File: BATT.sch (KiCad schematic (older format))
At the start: 7 parts

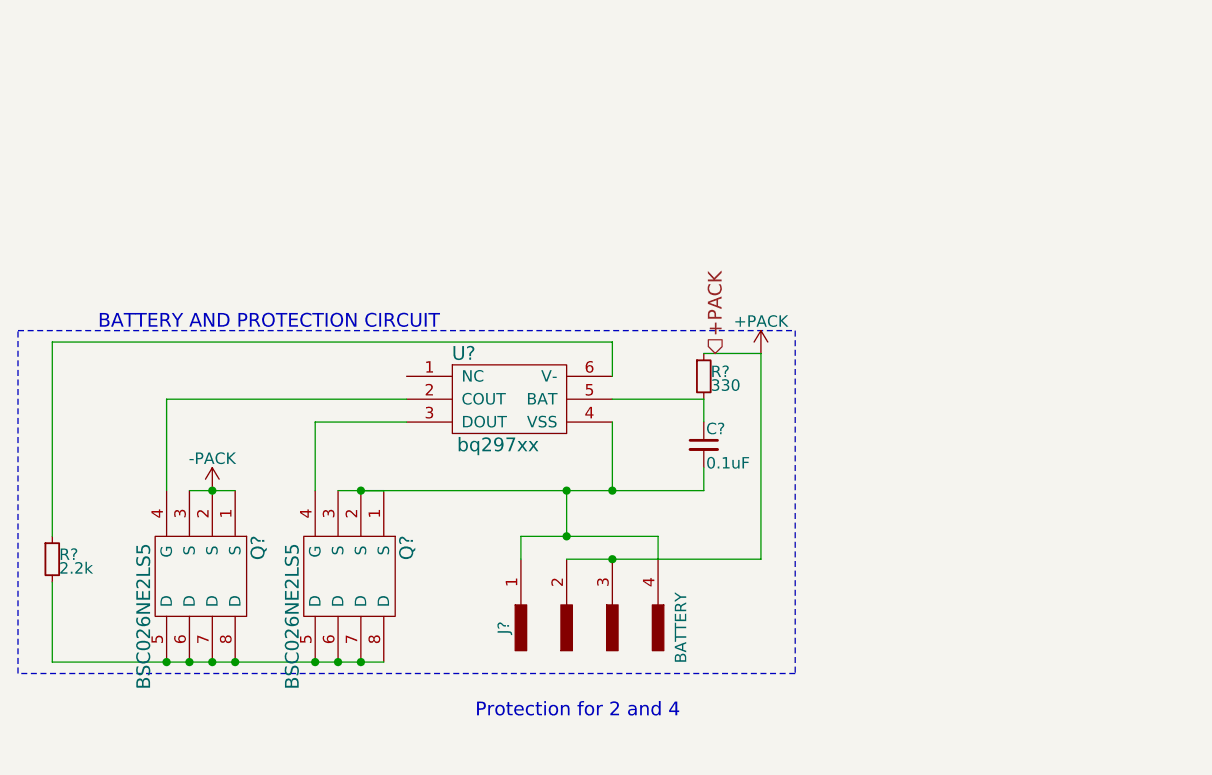
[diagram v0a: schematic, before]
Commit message: (Confirmation) BPack Ammeter + Proctection Circuit Edit
Making sure the last commit pushed all edits.
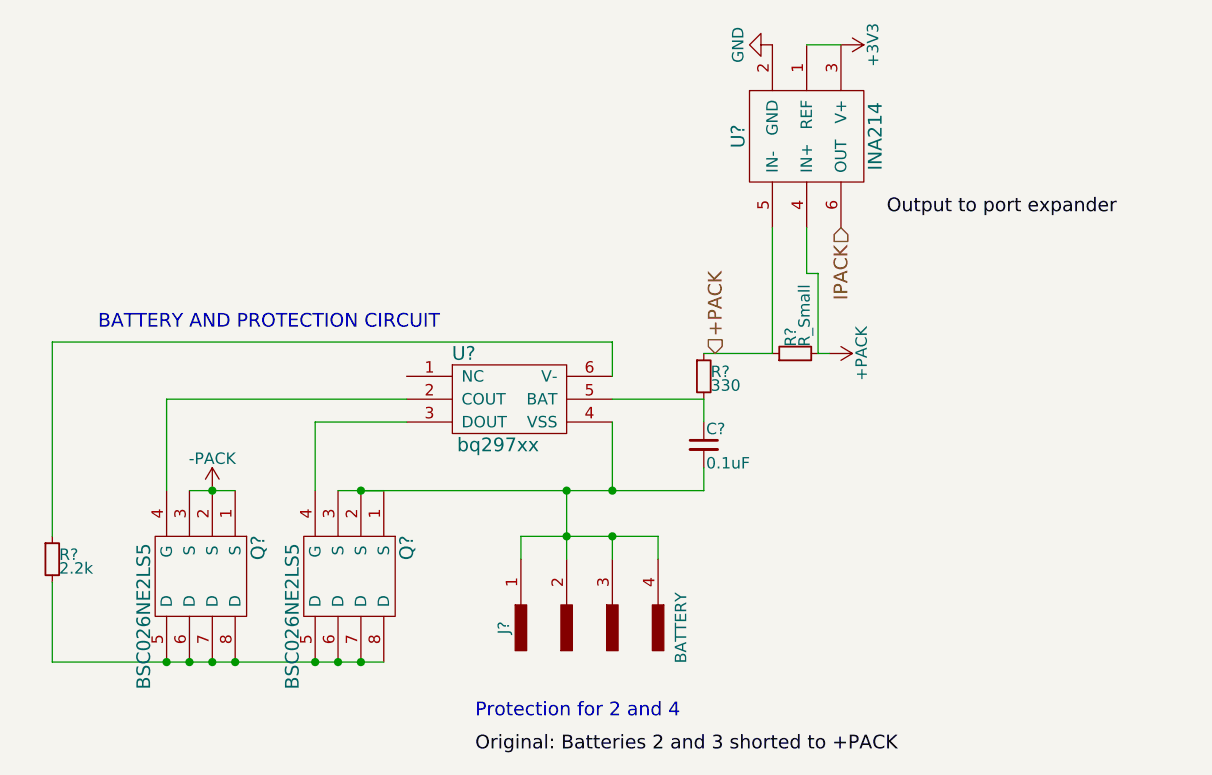
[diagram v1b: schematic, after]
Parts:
- added R?: R_Small, symbol R_Small
- added U?: INA214, symbol INA214
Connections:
- net +PACK: now also R?.1, R?.2, U?.4 (IN+), U?.5 (IN-); no longer J?.2, J?.3
- net at C?.2, J?.1, J?.4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: now also J?.2, J?.3
- new net +3V3: U?.1 (REF), U?.3 (V+)
- new net GND: U?.2 (GND)
- new net IPACK: U?.6 (OUT)
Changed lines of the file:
@@
 L +PACK #PWR?
 U 1 1 59EA52CA
-P 6750 2550
-F 0 "#PWR?" H 6750 2400 50  0001 C CNN
-F 1 "+PACK" H 6750 2690 50  0000 C CNN
-F 2 "" H 6750 2550 50  0001 C CNN
-F 3 "" H 6750 2550 50  0001 C CNN
-	1    6750 2550
-	1    0    0    -1
+P 7050 2550
+F 0 "#PWR?" H 7050 2400 50  0001 C CNN
+F 1 "+PACK" H 7050 2690 50  0000 C CNN
+F 2 "" H 7050 2550 50  0001 C CNN
+F 3 "" H 7050 2550 50  0001 C CNN
+	1    7050 2550
+	0    1    1    0
 $EndComp
 Text Notes 3850 2450 0    60   ~ 0
@@
 	6100 2500 6100 2650
 Wire Wire Line
-	5900 3150 5900 3350
+	5900 3150 5900 3450
 Connection ~ 5900 3150
-Wire Wire Line
-	6750 3450 6750 2550
-Wire Wire Line
-	6750 2550 6500 2550
-Connection ~ 6100 3450
 Wire Wire Line
 	6100 2850 6100 3150
 Connection ~ 6100 3150
-Wire Notes Line
-	3500 3950 3500 2450
-Wire Notes Line
-	3500 2450 6900 2450
-Wire Notes Line
-	6900 2450 6900 3950
-Wire Notes Line
-	6900 3950 3500 3950
-Wire Wire Line
-	5900 3450 6750 3450
 Text HLabel 6550 2550 1    60   Input ~ 0
 +PACK
 Text Notes 5500 4150 0    60   ~ 0
 Protection for 2 and 4
+$Comp
+L INA214 U?
+U 1 1 5A10F7B5
+P 6950 1600
+F 0 "U?" H 6950 1300 60  0000 C CNN
+F 1 "INA214" H 6950 1900 60  0000 C CNN
+F 2 "" H 6950 1900 60  0001 C CNN
+F 3 "" H 6950 1900 60  0001 C CNN
+	1    6950 1600
+	0    1    1    0
+$EndComp
+Text Label 5500 4300 0    60   ~ 0
+Original: Batteries 2 and 3 shorted to +PACK
+Wire Wire Line
+	6100 3350 6100 3450
+Connection ~ 6100 3350
+$Comp
+L R_Small R?
+U 1 1 5A112EB5
+P 6900 2550
+F 0 "R?" H 6930 2570 50  0000 L CNN
+F 1 "R_Small" H 6930 2510 50  0000 L CNN
+F 2 "" H 6900 2550 50  0001 C CNN
+F 3 "" H 6900 2550 50  0001 C CNN
+	1    6900 2550
+	0    -1   -1   0
+$EndComp
+Wire Wire Line
+	7000 2550 7050 2550
+Wire Wire Line
+	6500 2550 6800 2550
+Wire Wire Line
+	6800 2550 6800 2000
+Wire Wire Line
+	6950 1200 7100 1200
+$Comp
+L +3V3 #PWR?
+U 1 1 5A113C8A
+P 7100 1200
+F 0 "#PWR?" H 7100 1050 50  0001 C CNN
+F 1 "+3V3" H 7100 1340 50  0000 C CNN
+F 2 "" H 7100 1200 50  0001 C CNN
+F 3 "" H 7100 1200 50  0001 C CNN
+	1    7100 1200
+	0    1    1    0
+$EndComp
+$Comp
+L GND #PWR?
+U 1 1 5A113CE6
+P 6800 1200
+F 0 "#PWR?" H 6800 950 50  0001 C CNN
+F 1 "GND" H 6800 1050 50  0000 C CNN
+F 2 "" H 6800 1200 50  0001 C CNN
+F 3 "" H 6800 1200 50  0001 C CNN
+	1    6800 1200
+	0    1    1    0
+$EndComp
+Wire Wire Line
+	7000 2550 7000 2200
+Wire Wire Line
+	7000 2200 6950 2200
+Wire Wire Line
+	6950 2200 6950 2000
+Text HLabel 7100 2000 3    60   Input ~ 0
+IPACK
+Text Label 7300 1950 0    60   ~ 0
+Output to port expander
 $EndSCHEMATC

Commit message: Battery Pack Edits
- Fixed hierarchy label errors (output to input)
- Added Voltmeter to Battery Pack Schematic
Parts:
- added C?: C_Small, symbol C_Small
- added R? (x2): R_Small, symbol R_Small
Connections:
- net +PACK: now also R?.1; no longer R?.1, R?.1, U?.5 (IN-)
- net GND: now also C?.1, R?.2
- new net: R?.1, R?.1, U?.5 (IN-)
- new net VPack: C?.2, R?.1, R?.2
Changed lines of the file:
@@
 L +PACK #PWR?
 U 1 1 59EA52CA
-P 7050 2550
-F 0 "#PWR?" H 7050 2400 50  0001 C CNN
-F 1 "+PACK" H 7050 2690 50  0000 C CNN
-F 2 "" H 7050 2550 50  0001 C CNN
-F 3 "" H 7050 2550 50  0001 C CNN
-	1    7050 2550
+P 7550 2550
+F 0 "#PWR?" H 7550 2400 50  0001 C CNN
+F 1 "+PACK" H 7550 2690 50  0000 C CNN
+F 2 "" H 7550 2550 50  0001 C CNN
+F 3 "" H 7550 2550 50  0001 C CNN
+	1    7550 2550
 	0    1    1    0
 $EndComp
 Text Notes 3850 2450 0    60   ~ 0
 BATTERY AND PROTECTION CIRCUIT
+Text HLabel 7550 2550 1    60   Output ~ 0
++PACK
+Text Notes 5500 4150 0    60   ~ 0
+Protection for 2 and 4
+$Comp
+L INA214 U?
+U 1 1 5A10F7B5
+P 6950 1600
+F 0 "U?" H 6950 1300 60  0000 C CNN
+F 1 "INA214" H 6950 1900 60  0000 C CNN
+F 2 "" H 6950 1900 60  0001 C CNN
+F 3 "" H 6950 1900 60  0001 C CNN
+	1    6950 1600
+	0    1    1    0
+$EndComp
+Text Label 5500 4300 0    60   ~ 0
+Original: Batteries 2 and 3 shorted to +PACK
+$Comp
+L R_Small R?
+U 1 1 5A112EB5
+P 6900 2550
+F 0 "R?" H 6930 2570 50  0000 L CNN
+F 1 "R_Small" H 6930 2510 50  0000 L CNN
+F 2 "" H 6900 2550 50  0001 C CNN
+F 3 "" H 6900 2550 50  0001 C CNN
+	1    6900 2550
+	0    -1   -1   0
+$EndComp
+$Comp
+L +3V3 #PWR?
+U 1 1 5A113C8A
+P 7100 1200
+F 0 "#PWR?" H 7100 1050 50  0001 C CNN
+F 1 "+3V3" H 7100 1340 50  0000 C CNN
+F 2 "" H 7100 1200 50  0001 C CNN
+F 3 "" H 7100 1200 50  0001 C CNN
+	1    7100 1200
+	0    1    1    0
+$EndComp
+$Comp
+L GND #PWR?
+U 1 1 5A113CE6
+P 6800 1200
+F 0 "#PWR?" H 6800 950 50  0001 C CNN
+F 1 "GND" H 6800 1050 50  0000 C CNN
+F 2 "" H 6800 1200 50  0001 C CNN
+F 3 "" H 6800 1200 50  0001 C CNN
+	1    6800 1200
+	0    1    1    0
+$EndComp
+Text HLabel 7100 2000 3    60   Input ~ 0
+IPACK
+Text Label 7300 1950 0    60   ~ 0
+Output to port expander
+$Comp
+L R_Small R?
+U 1 1 5A19EE91
+P 7350 2750
+F 0 "R?" H 7400 2800 50  0000 L CNN
+F 1 "R_Small" H 7380 2710 50  0000 L CNN
+F 2 "" H 7350 2750 50  0001 C CNN
+F 3 "" H 7350 2750 50  0001 C CNN
+	1    7350 2750
+	1    0    0    -1
+$EndComp
+$Comp
+L R_Small R?
+U 1 1 5A19EED2
+P 7350 3050
+F 0 "R?" H 7400 3100 50  0000 L CNN
+F 1 "R_Small" H 7380 3010 50  0000 L CNN
+F 2 "" H 7350 3050 50  0001 C CNN
+F 3 "" H 7350 3050 50  0001 C CNN
+	1    7350 3050
+	1    0    0    -1
+$EndComp
+$Comp
+L C_Small C?
+U 1 1 5A19EF38
+P 7150 2900
+F 0 "C?" H 7160 2970 50  0000 L CNN
+F 1 "C_Small" H 7160 2820 50  0000 L CNN
+F 2 "" H 7150 2900 50  0001 C CNN
+F 3 "" H 7150 2900 50  0001 C CNN
+	1    7150 2900
+	0    -1   -1   0
+$EndComp
+$Comp
+L GND #PWR?
+U 1 1 5A19EF85
+P 7050 3150
+F 0 "#PWR?" H 7050 2900 50  0001 C CNN
+F 1 "GND" H 7050 3000 50  0000 C CNN
+F 2 "" H 7050 3150 50  0001 C CNN
+F 3 "" H 7050 3150 50  0001 C CNN
+	1    7050 3150
+	1    0    0    -1
+$EndComp
 Wire Wire Line
 	3650 3900 5100 3900
@@
 	6100 2850 6100 3150
 Connection ~ 6100 3150
-Text HLabel 6550 2550 1    60   Input ~ 0
-+PACK
-Text Notes 5500 4150 0    60   ~ 0
-Protection for 2 and 4
-$Comp
-L INA214 U?
-U 1 1 5A10F7B5
-P 6950 1600
-F 0 "U?" H 6950 1300 60  0000 C CNN
-F 1 "INA214" H 6950 1900 60  0000 C CNN
-F 2 "" H 6950 1900 60  0001 C CNN
-F 3 "" H 6950 1900 60  0001 C CNN
-	1    6950 1600
-	0    1    1    0
-$EndComp
-Text Label 5500 4300 0    60   ~ 0
-Original: Batteries 2 and 3 shorted to +PACK
 Wire Wire Line
 	6100 3350 6100 3450
 Connection ~ 6100 3350
-$Comp
-L R_Small R?
-U 1 1 5A112EB5
-P 6900 2550
-F 0 "R?" H 6930 2570 50  0000 L CNN
-F 1 "R_Small" H 6930 2510 50  0000 L CNN
-F 2 "" H 6900 2550 50  0001 C CNN
-F 3 "" H 6900 2550 50  0001 C CNN
-	1    6900 2550
-	0    -1   -1   0
-$EndComp
 Wire Wire Line
-	7000 2550 7050 2550
+	7000 2550 7550 2550
 Wire Wire Line
 	6500 2550 6800 2550
@@
 Wire Wire Line
 	6950 1200 7100 1200
-$Comp
-L +3V3 #PWR?
-U 1 1 5A113C8A
-P 7100 1200
-F 0 "#PWR?" H 7100 1050 50  0001 C CNN
-F 1 "+3V3" H 7100 1340 50  0000 C CNN
-F 2 "" H 7100 1200 50  0001 C CNN
-F 3 "" H 7100 1200 50  0001 C CNN
-	1    7100 1200
-	0    1    1    0
-$EndComp
-$Comp
-L GND #PWR?
-U 1 1 5A113CE6
-P 6800 1200
-F 0 "#PWR?" H 6800 950 50  0001 C CNN
-F 1 "GND" H 6800 1050 50  0000 C CNN
-F 2 "" H 6800 1200 50  0001 C CNN
-F 3 "" H 6800 1200 50  0001 C CNN
-	1    6800 1200
-	0    1    1    0
-$EndComp
 Wire Wire Line
 	7000 2550 7000 2200
@@
 Wire Wire Line
 	6950 2200 6950 2000
-Text HLabel 7100 2000 3    60   Input ~ 0
-IPACK
-Text Label 7300 1950 0    60   ~ 0
-Output to port expander
+Wire Wire Line
+	7350 2550 7350 2650
+Connection ~ 7350 2550
+Wire Wire Line
+	7350 2850 7350 2950
+Wire Wire Line
+	7250 2900 7600 2900
+Connection ~ 7350 2900
+Wire Wire Line
+	7050 2900 7050 3150
+Wire Wire Line
+	7050 3150 7350 3150
+Text HLabel 7600 2900 2    60   Output ~ 0
+VPack
 $EndSCHEMATC
